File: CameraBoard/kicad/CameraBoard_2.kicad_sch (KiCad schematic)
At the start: 39 parts, among them Q2 BVSS123LT1G, Q3 BSS84, U4 TS5A3159ADBVR, U5 ICM7242IBAZ-SMD, U6 H11F1SR2M, U7 H11F1SR2M, U8 SN74LVC1G17DCKR

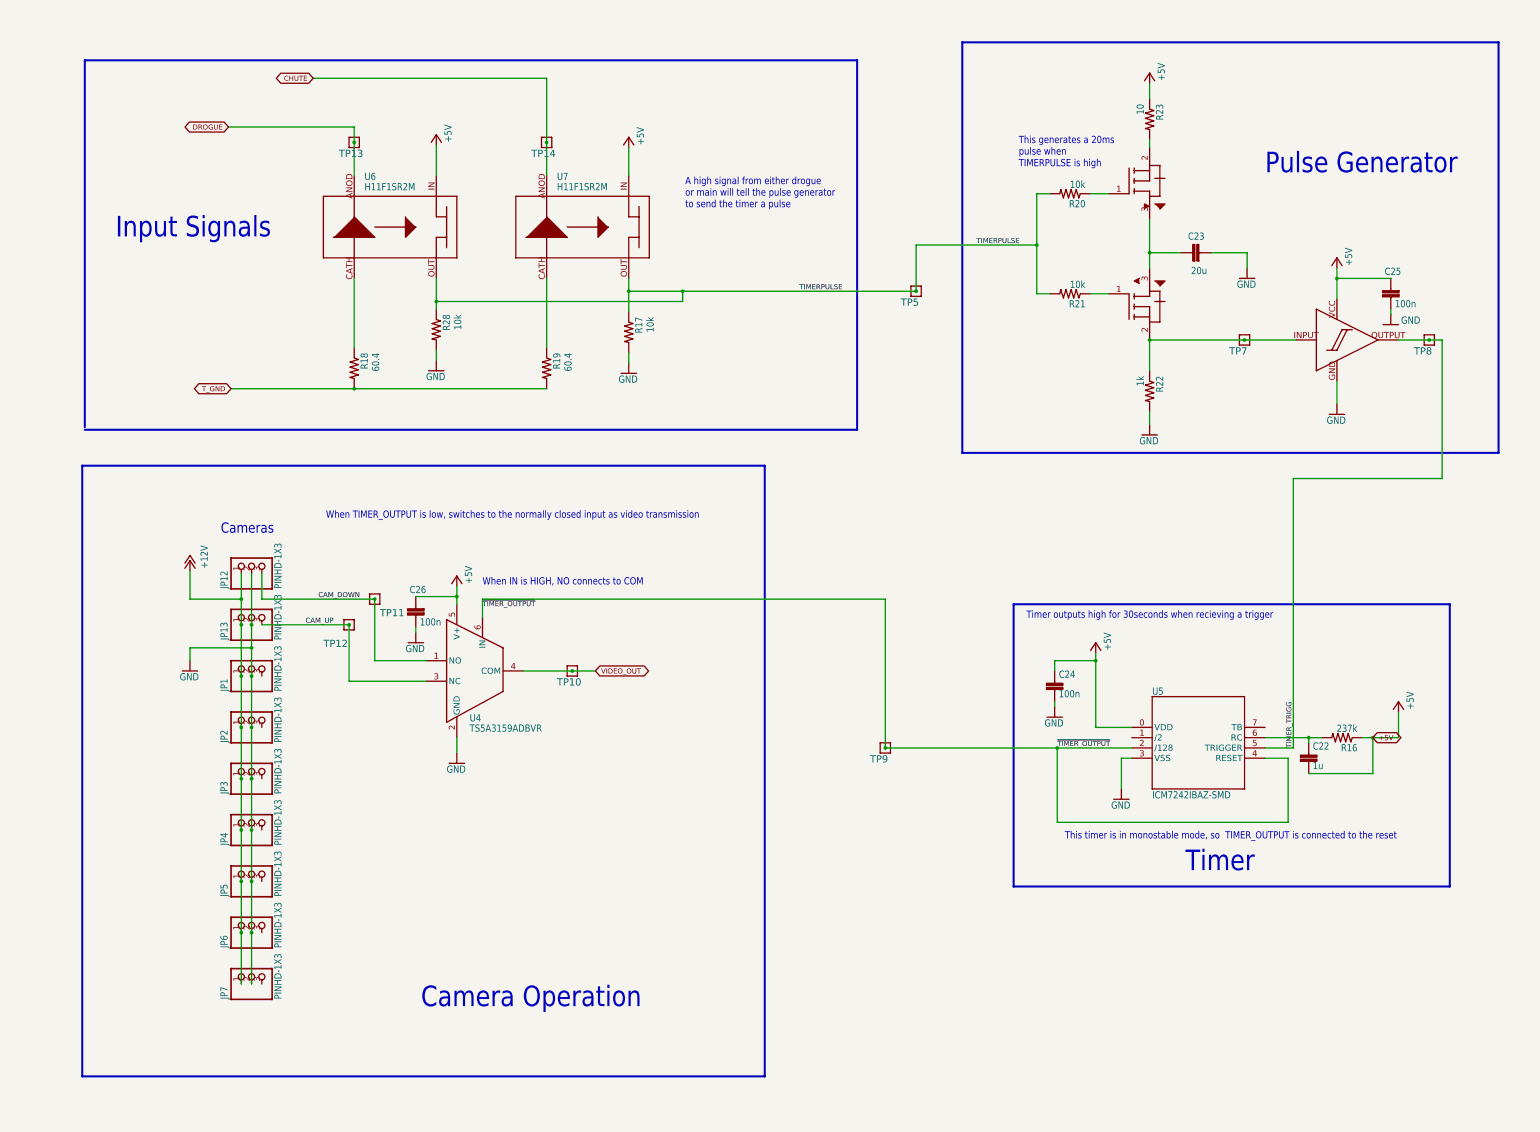
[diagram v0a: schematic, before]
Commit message: Cleaned up second page - fixed optoisolator symbols, added notes about levels and times, and cleaned up alot. Put in notes about mod wires.
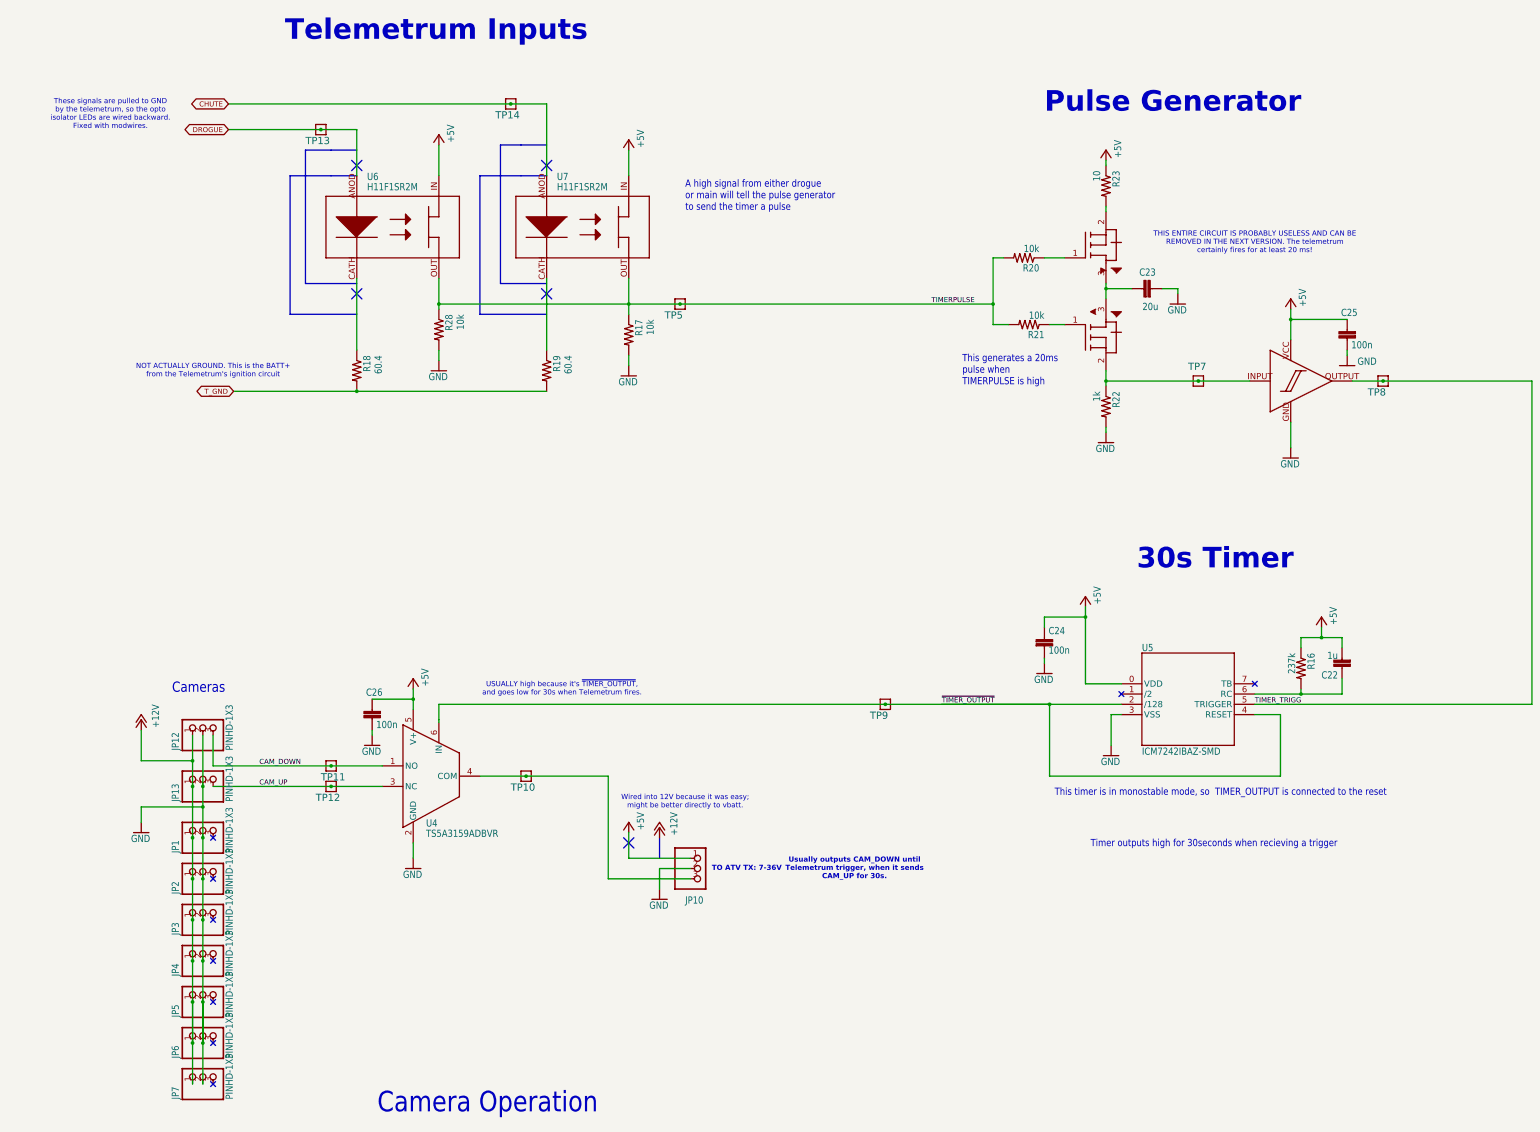
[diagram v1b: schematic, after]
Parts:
- added JP10: PINHD-1X3, CameraBoard:1X03, symbol CameraBoard-eagle-import:PINHD-1X3
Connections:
- net +5V: now also JP10.1
- net GND: now also JP10.2
- net VIDEO_OUT: no longer names the net of TP10.1, U4.4 (COM)
- net VIDEO_OUT: now also JP10.3
- no-connect marks 0 -> 9
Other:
- note added: "30s Timer"
- note added: "NOT ACTUALLY GROUND. This is the BATT+ from the Telemetrum's ignition circuit"
- note added: "THIS ENTIRE CIRCUIT IS PROBABLY USELESS AND CAN BE REMOVED IN THE NEXT VERSION. The telemetrum certainly fires for at least 20 ms!"
- note added: "TO ATV TX: 7-36V"
- note added: "Telemetrum Inputs"
- note added: "These signals are pulled to GND by the telemetrum, so the opto isolator LEDs are wired backward. Fixed with modwires."
- note added: "USUALLY high because it's ~{TIMER_OUTPUT}, and goes low for 30s when Telemetrum fires."
- note added: "Usually outputs CAM_DOWN until Telemetrum trigger, when it sends CAM_UP for 30s."
- note added: "Wired into 12V because it was easy; might be better directly to vbatt."
- note removed: "Input Signals"
- note removed: "Timer"
- note removed: "When IN is HIGH, NO connects to COM"
- note removed: "When TIMER_OUTPUT is low, switches to the normally closed input as video transmission"
- moved on the sheet: C22, C23, C24, C25, C26, JP1, JP12, JP13, JP2, JP3, JP4, JP5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

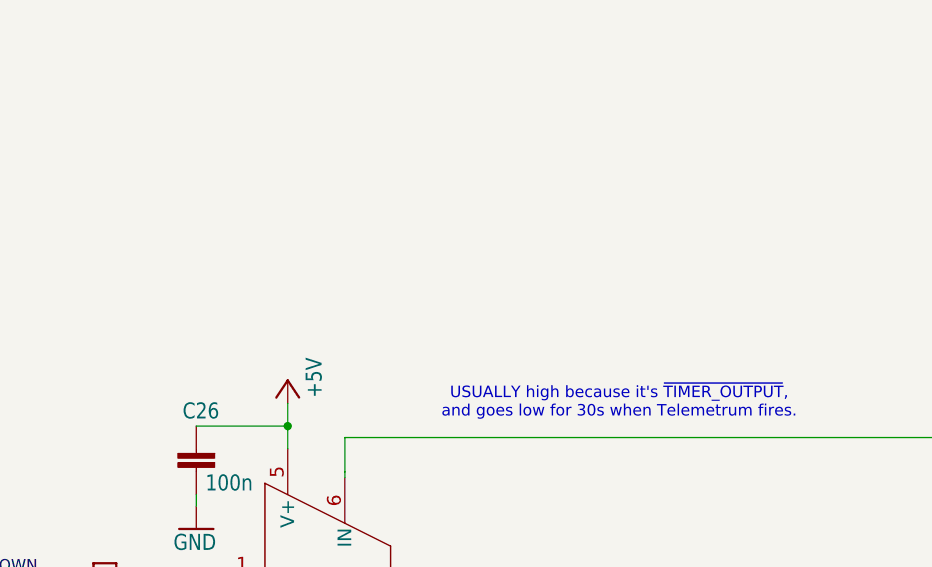
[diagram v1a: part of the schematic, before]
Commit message: Make schematic better, mostly cleaning up EAGLE import errors
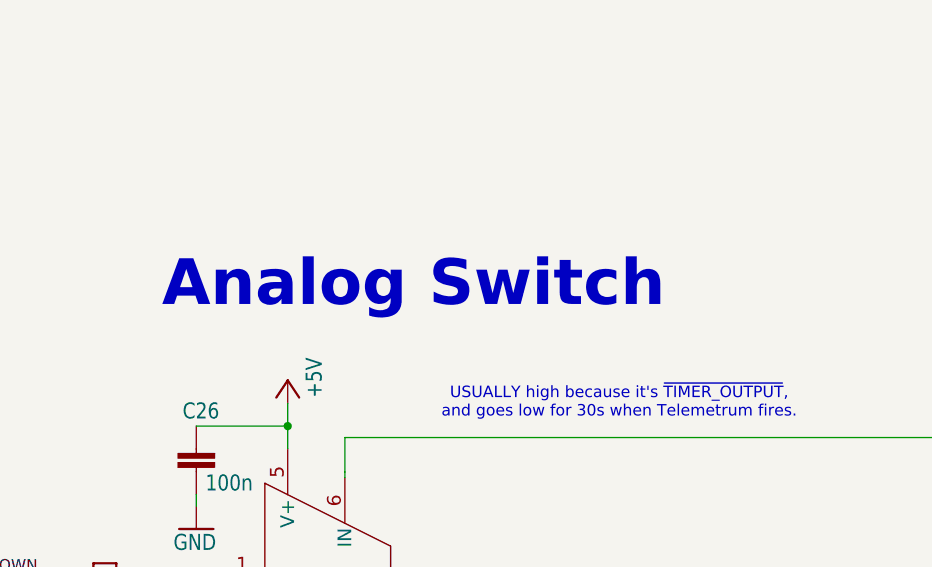
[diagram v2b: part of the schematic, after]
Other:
- note added: "Analog Switch"
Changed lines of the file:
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@@
+		)
+	)
+	(text "Analog Switch"
+		(exclude_from_sim no)
+		(at 129.54 179.07 0)
+		(effects
+			(font
+				(size 5.08 5.08)
+				(thickness 1.016)
+				(bold yes)
+			)
+			(justify left bottom)
 		)
 	)

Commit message: Minor updates to PCB
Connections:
- net +12V: now also JP10.1
- net +5V: no longer JP10.1
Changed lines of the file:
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@@
 	(wire
 		(pts
-			(xy 196.85 231.14) (xy 212.09 231.14)
-		)
-		(stroke
-			(width 0.1524)
-			(type solid)
-		)
-	)
-	(wire
-		(pts
 			(xy 191.77 236.22) (xy 212.09 236.22)
 		)
@@
 	(wire
 		(pts
+			(xy 204.47 226.06) (xy 204.47 231.14)
+		)
+		(stroke
+			(width 0)
+			(type default)
+		)
+	)
+	(wire
+		(pts
 			(xy 88.9 200.66) (xy 88.9 207.01)
 		)
@@
 	(wire
 		(pts
-			(xy 196.85 224.79) (xy 196.85 231.14)
-		)
-		(stroke
-			(width 0.1524)
-			(type solid)
-		)
-	)
-	(wire
-		(pts
 			(xy 299.72 182.88) (xy 299.72 181.61)
 		)
@@
 	(wire
 		(pts
+			(xy 212.09 231.14) (xy 204.47 231.14)
+		)
+		(stroke
+			(width 0)
+			(type default)
+		)
+	)
+	(wire
+		(pts
 			(xy 88.9 207.01) (xy 88.9 213.36)
 		)
@@
 	(polyline
 		(pts
-			(xy 195.58 226.06) (xy 198.12 228.6)
-		)
-		(stroke
-			(width 0.254)
-			(type solid)
-			(color 255 0 0 1)
-		)
-	)
-	(polyline
-		(pts
 			(xy 116.84 88.9) (xy 129.54 88.9)
 		)
@@
 		)
 	)
-	(polyline
-		(pts
-			(xy 195.58 228.6) (xy 198.12 226.06)
-		)
-		(stroke
-			(width 0.254)
-			(type solid)
-			(color 255 0 0 1)
-		)
-	)
 	(wire
 		(pts
@@
 		)
 	)
-	(polyline
-		(pts
-			(xy 204.47 231.14) (xy 204.47 226.06)
-		)
-		(stroke
-			(width 0.254)
-			(type solid)
-			(color 255 0 0 1)
-		)
-	)
 	(wire
 		(pts
@@
 					(unit 1)
 				)
-			)
-		)
-	)
-	(symbol
-		(lib_id "CameraBoard-eagle-import:+5V")
-		(at 196.85 222.25 0)
-		(unit 1)
-		(exclude_from_sim no)
-		(in_bom yes)
-		(on_board yes)
-		(dnp no)
-		(property "Reference" "#P+2"
-			(at 196.85 222.25 0)
-			(effects
-				(font
-					(size 1.27 1.27)
-				)
-				(hide yes)
-			)
-		)
-		(property "Value" "+5V"
-			(at 198.755 219.71 90)
-			(effects
-				(font
-					(size 1.778 1.5113)
-				)
-				(justify right top)
-			)
-		)
-		(property "Footprint" ""
-			(at 196.85 222.25 0)
-			(effects
-				(font
-					(size 1.27 1.27)
-				)
-				(hide yes)
-			)
-		)
-		(property "Datasheet" ""
-			(at 196.85 222.25 0)
-			(effects
-				(font
-					(size 1.27 1.27)
-				)
-				(hide yes)
-			)
-		)
-		(property "Description" ""
-			(at 196.85 222.25 0)
-			(effects
-				(font
-					(size 1.27 1.27)
-				)
-				(hide yes)
-			)
-		)
-		(pin "1"
-		)
-		(instances
-			(project "CameraBoard"
-				(path "/876601fa-fbd1-4e2d-9c28-84441865735b/537433a0-7b0a-4286-9b5c-a2c4a7e302ab"
-					(reference "#P+2")
-					(unit 1)
-				)
